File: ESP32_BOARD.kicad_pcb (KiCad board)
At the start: 2 copper layers, 56.8 x 103 mm, 66 parts, among them IC1 AP2112K-3.3, IC2 MPQ4420HGJ-Z, IC3 W25Q128JVSIQ, IC4 ESP32-S3R8, IC5 AW9364DNR, Q1 40MHz, SW1 TS-1010B-B-A, SW2 PTS810SJK250SMTRLFS, SW3 PTS810SJK250SMTRLFS

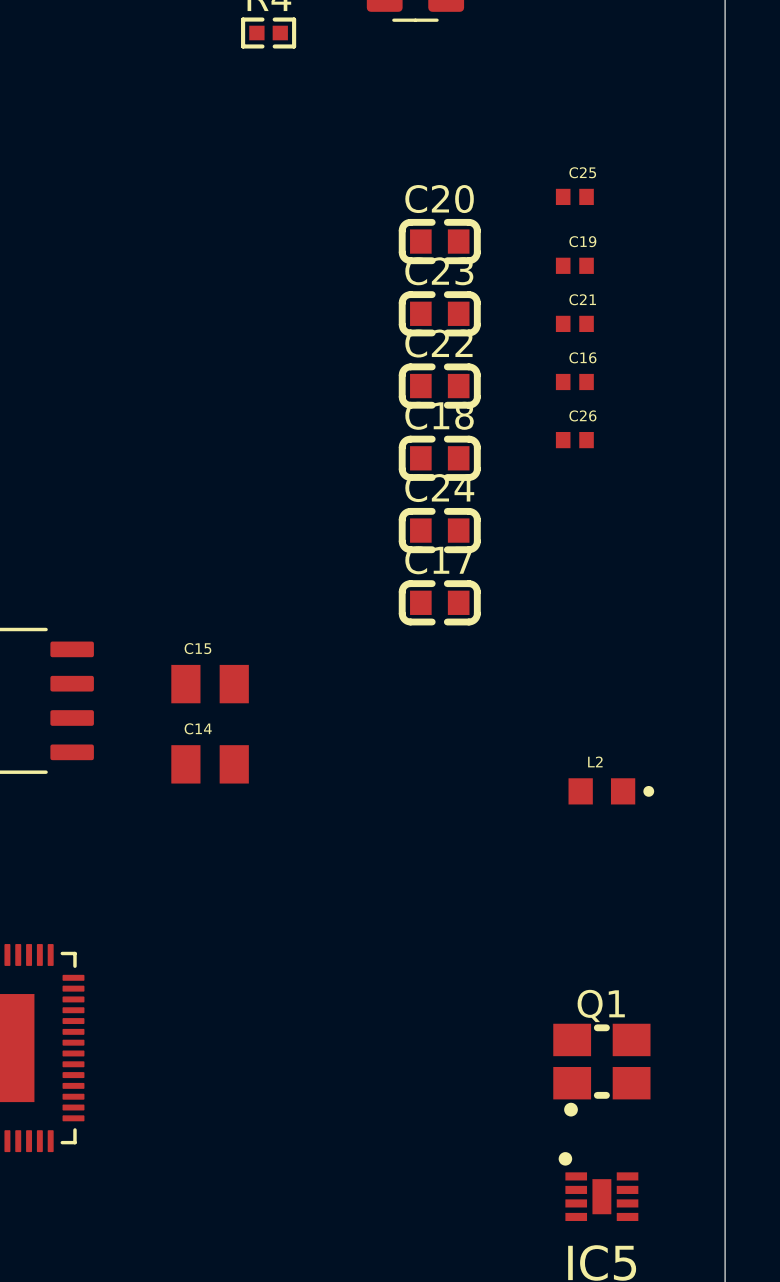
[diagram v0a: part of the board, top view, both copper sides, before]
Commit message: Crystal Change
Crystal changed from active (CMSO) to passive with 2x 15pF load capacitors
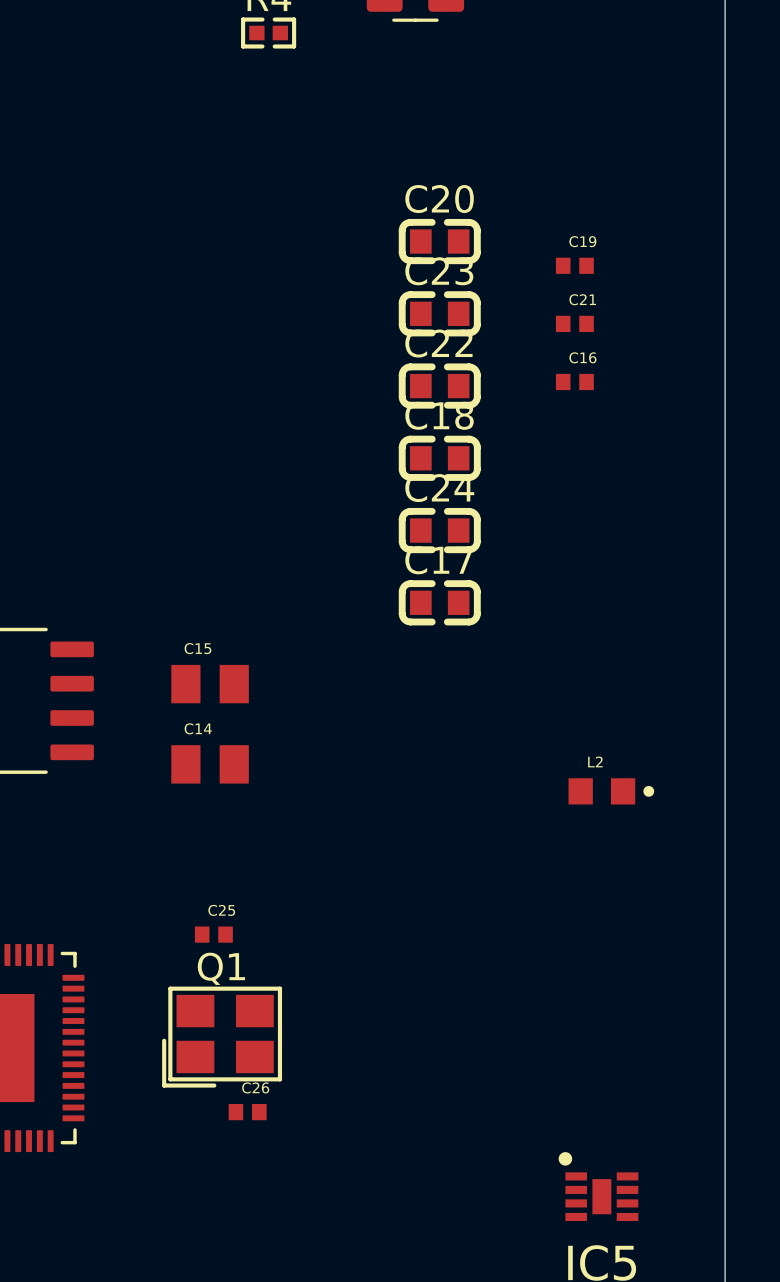
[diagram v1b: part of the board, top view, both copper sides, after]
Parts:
- C26: value 12pF -> 15pF; footprint GRM1555C1H120JA01D:CAPC1005X55N -> GRM1555C1H150JA01D:CAPC1005X55N
- Q1: footprint S3D40.000000B20F30T:OSC-SMD_4P-L3.2-W2.5-BL-1 -> S3240000151040:CRYSTAL-SMD_4P-L3.2-W2.5-BL
- moved C25 30.4 mm to (115.2, 103.6)
- moved C26 27.7 mm to (116.5, 110.2)
- moved Q1 14.0 mm to (115.7, 107.3)
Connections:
- Q1 pad 1: /Microcontroller/XTAL_N -> /Microcontroller/XTAL_P
- Q1 pad 3: /Microcontroller/XTAL_P -> /Microcontroller/XTAL_N

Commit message: Changes to final schematic
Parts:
- added D1: APHHS1005CGCK, APHHS1005CGCK:LED_APHHS1005CGCK, F.Cu at (128.9, 63.0)
- added R15: 220, RC0402FR-07220RL:RESC1005X40N, F.Cu at (128.9, 65.1)
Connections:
- net ESP_USB_DM renamed ESP_USB_D-
- net ESP_USB_DP renamed ESP_USB_D+
- Q1 pad 1: /Microcontroller/XTAL_P -> /Microcontroller/XTAL_N
- Q1 pad 3: /Microcontroller/XTAL_N -> /Microcontroller/XTAL_P

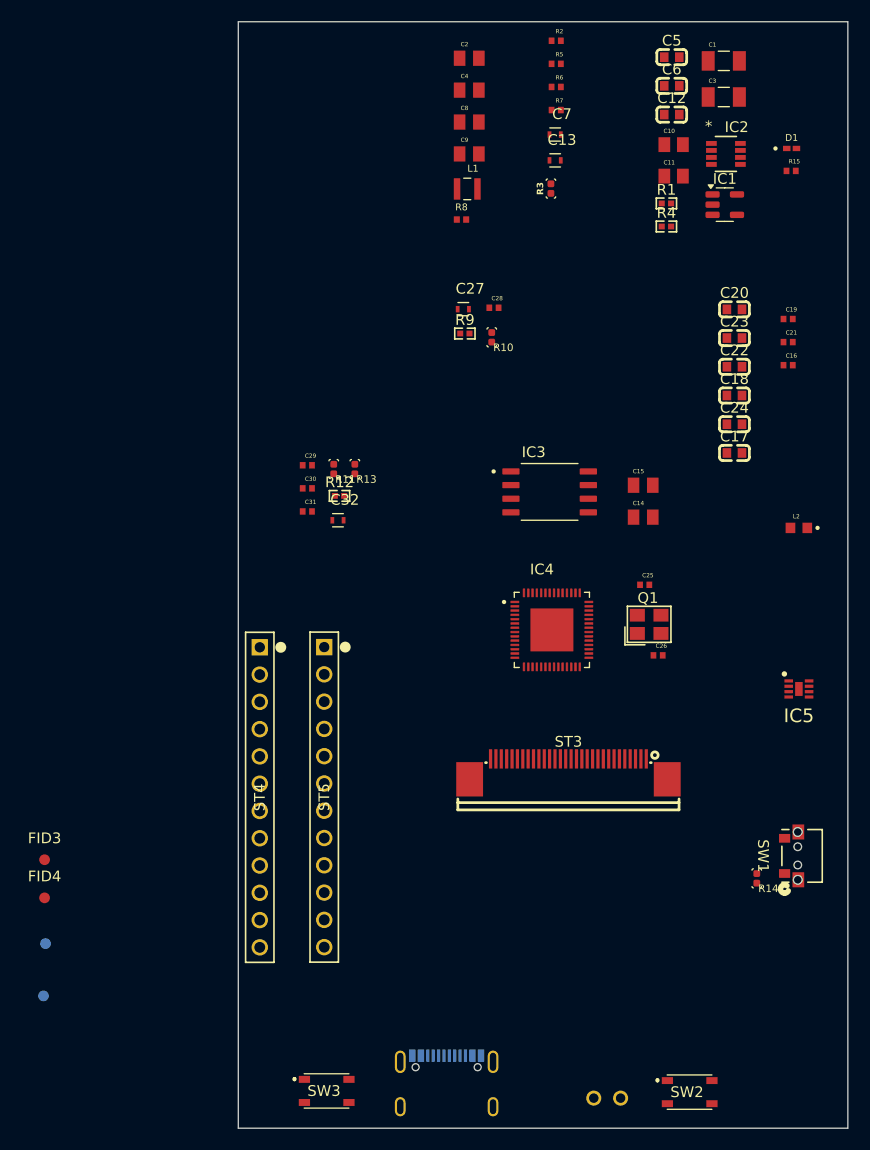
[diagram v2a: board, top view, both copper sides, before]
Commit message: Layout Started
Board setup done, DC/DC Converters arranged and slight changes tot he board outline.
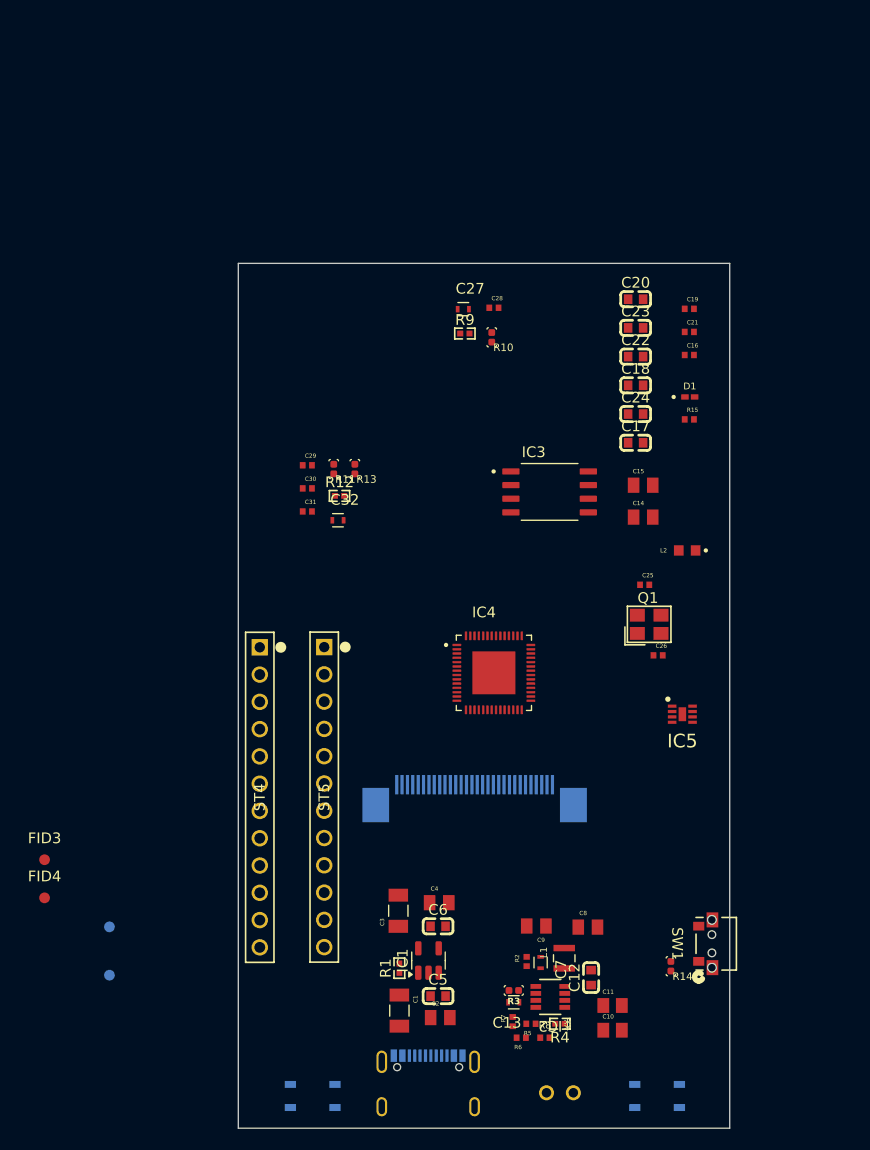
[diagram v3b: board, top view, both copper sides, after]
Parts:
- ST3, SW2, SW3: moved to B.Cu
- moved C1 93.5 mm to (92.4, 143.2), turned to -90 degrees
- moved C5 90.1 mm to (96.0, 141.9)
- moved R5 89.4 mm to (104.7, 144.5), turned to 180 degrees
- moved C2 89.4 mm to (96.2, 143.9)
- moved R6 88.6 mm to (103.8, 145.8), turned to 180 degrees
- moved R2 85.8 mm to (104.3, 138.7), turned to 90 degrees
- moved R7 85.0 mm to (103.0, 144.3), turned to 90 degrees
- moved C10 82.7 mm to (112.3, 145.1)
- moved C3 81.6 mm to (92.3, 133.9), turned to 90 degrees
- moved C6 81.2 mm to (96.0, 135.4)
- moved C12 80.7 mm to (110.3, 140.2), turned to 90 degrees
- moved IC2 80.2 mm to (106.5, 142.0), turned to 180 degrees
- moved C13 78.5 mm to (103.1, 142.5), turned to 180 degrees
- moved C11 77.4 mm to (112.3, 142.8)
- moved C7 77.1 mm to (105.6, 138.8), turned to -90 degrees
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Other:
- board size 56.8 x 103 mm -> 45.8 x 80.5 mm
- copper layers 2 -> 4

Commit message: Arranged Headers + Added pull-down resistors for type-c conn
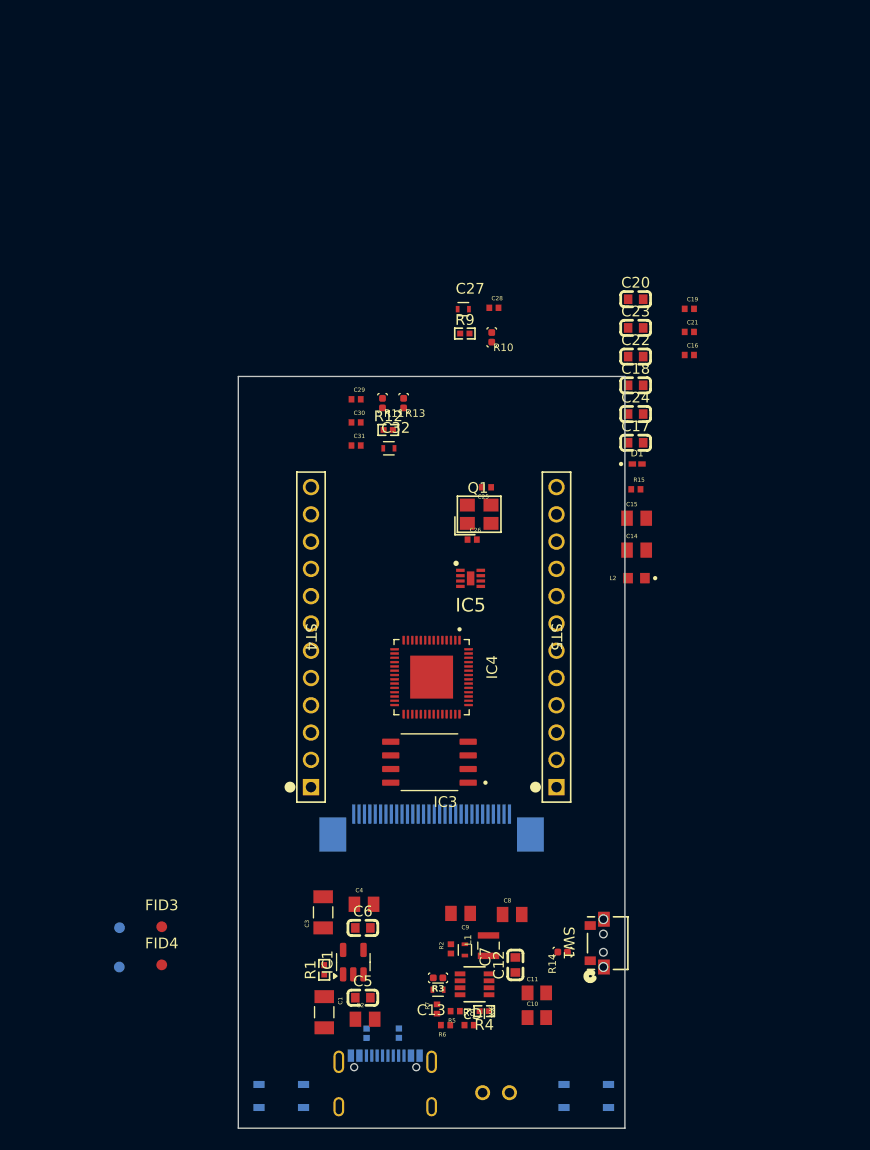
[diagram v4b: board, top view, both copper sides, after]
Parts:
- added R16: 5.1k, 0402WGF5101TCE:RESC1005X40N, B.Cu at (92.3, 145.3)
- added R17: 5.1k, 0402WGF5101TCE:RESC1005X40N, B.Cu at (89.3, 145.4)
- moved IC3 27.5 mm to (95.2, 120.1), turned to 180 degrees
- moved ST5 25.3 mm to (107.0, 122.4), turned to -90 degrees
- moved IC5 23.4 mm to (99.0, 103.0)
- moved C26 20.4 mm to (99.2, 99.4)
- moved Q1 18.9 mm to (99.8, 97.0)
- moved C25 17.3 mm to (100.5, 94.5), turned to 180 degrees
- moved ST4 13.9 mm to (84.2, 122.4), turned to -90 degrees
- moved FID3 12.6 mm to (70.3, 135.4)
- moved FID4 12.6 mm to (70.3, 139.0)
- moved R14 10.2 mm to (107.6, 137.8), turned to -90 degrees
- moved SW1 10.1 mm to (110.2, 138.6)
- moved C32 8.21 mm to (91.4, 90.9)
- moved R15 8.20 mm to (114.4, 94.7)
- moved D1 7.93 mm to (114.5, 92.3)
- moved C29 7.64 mm to (88.4, 86.3)
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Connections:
- ST2 pad A5: unconnected-(ST2-CC1-PadA5) -> /Input Connectors/CC1
- ST2 pad B5: unconnected-(ST2-CC2-PadB5) -> /Input Connectors/CC2
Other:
- board size 45.8 x 80.5 mm -> 36 x 70 mm

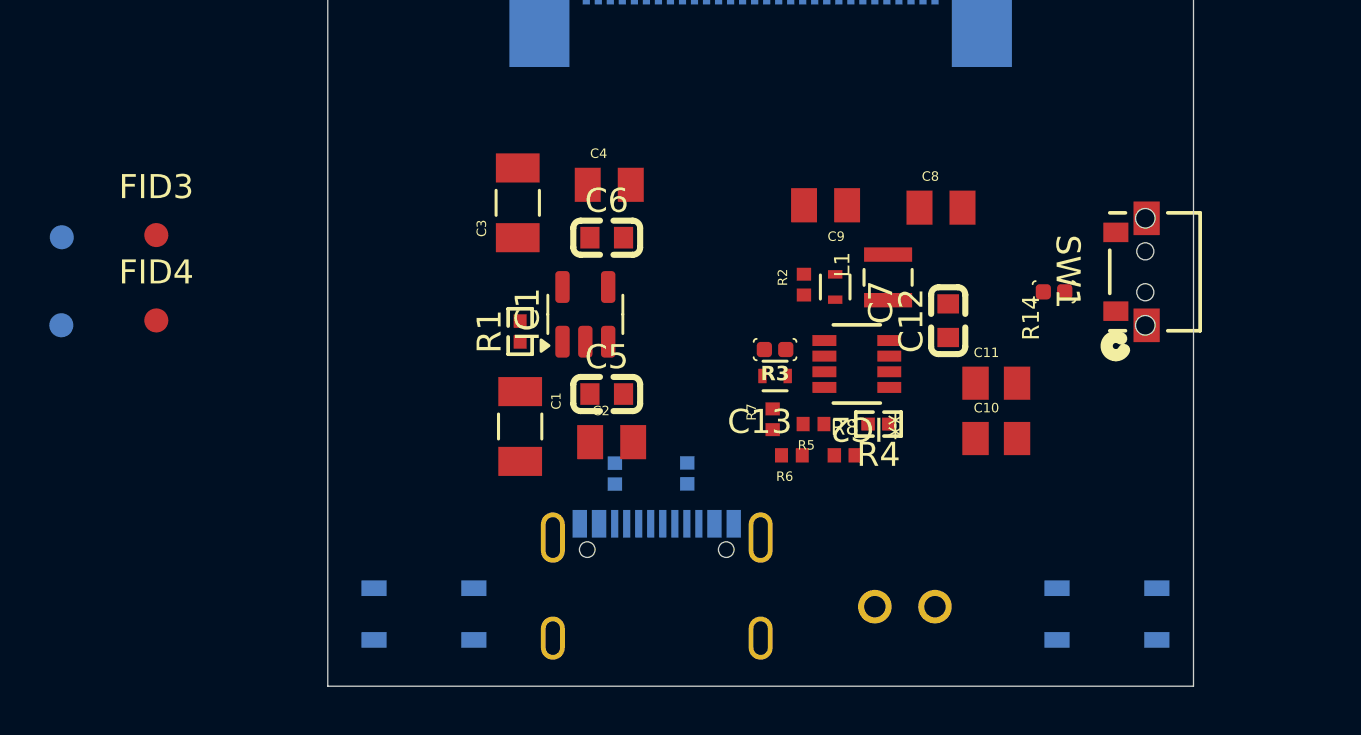
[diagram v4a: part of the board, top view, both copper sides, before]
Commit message: JST 2 PIN CONN Changed + Additional 3D Models added
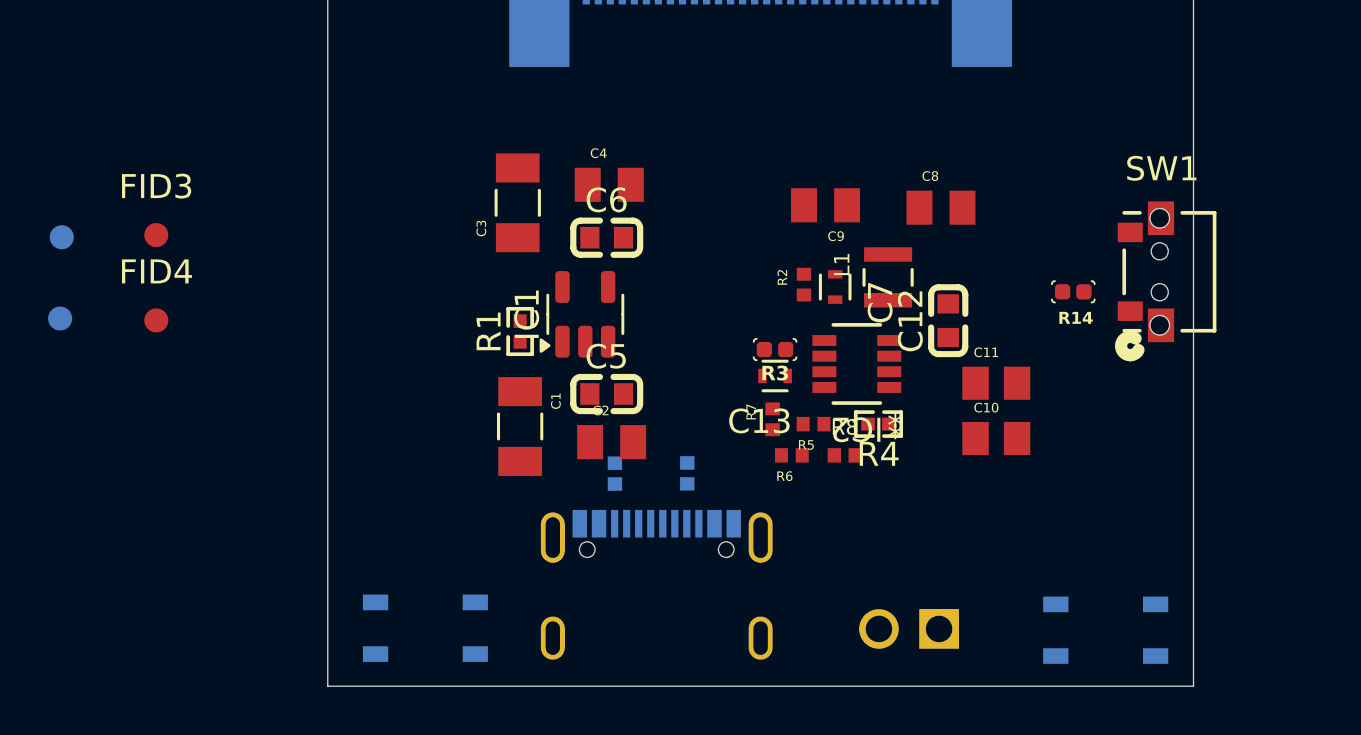
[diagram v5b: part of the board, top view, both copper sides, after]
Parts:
- ST1: value B2B-EH-A LFSN -> B2B-EH-A (LF)(SN); footprint JST_B2B-EH-A-LF-SN:CONN_B2B-EH-A LFSN_JST -> JST_B2B-EH-A(LF)(SN):SHDR2W64P0X250_1X2_750X380X600P
- moved ST1 0.94 mm to (102.8, 151.8)
- moved R14 0.80 mm to (108.4, 137.8)
- moved SW2 0.67 mm to (109.8, 151.9)
- moved SW1 0.60 mm to (110.8, 138.6)
- moved SW3 0.59 mm to (81.5, 151.8), turned to 0 degrees
- moved FID2 0.28 mm to (66.3, 138.9)
